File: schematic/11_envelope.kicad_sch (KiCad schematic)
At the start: 23 parts, among them Q601 2N7002, Q602 MMBT3904, Q603 BSS84, Q604 MMBT3904, Q605 2N7002, U601 TLC555IDR, U602 OPA4192IDR

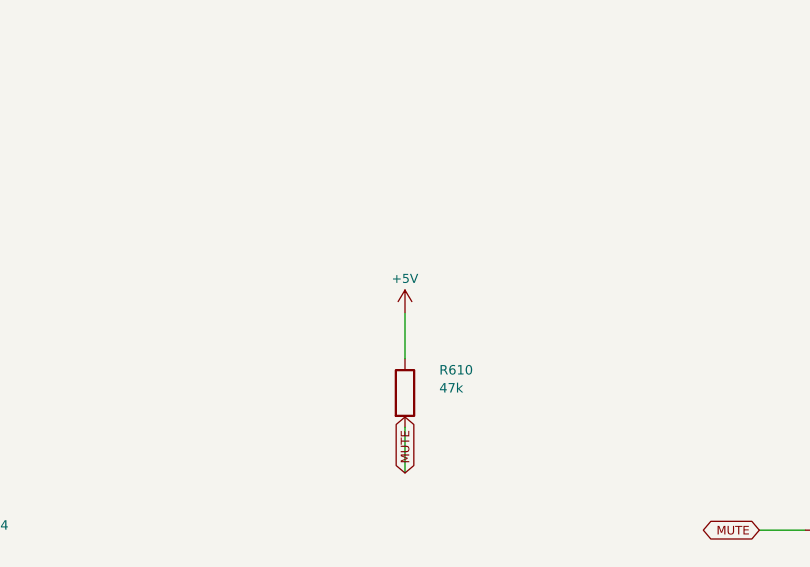
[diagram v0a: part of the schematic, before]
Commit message: add power supply, rail checks and parts list
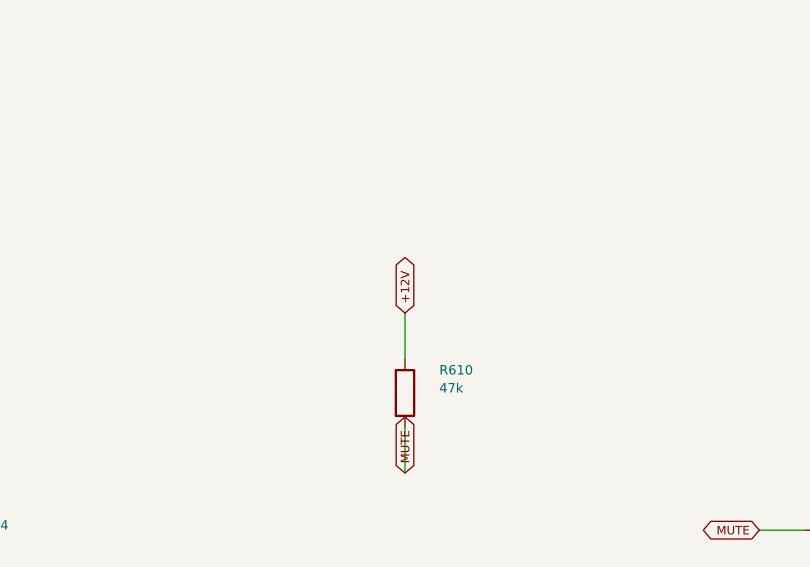
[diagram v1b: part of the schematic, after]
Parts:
- Q601, Q605: MPN (none) -> 2N7002,215; Manufacturer (none) -> Nexperia; Supplier (none) -> LCSC
- Q602, Q604: MPN (none) -> MMBT3904,215; Manufacturer (none) -> Nexperia; Supplier (none) -> LCSC
- Q603: MPN (none) -> BSS84,215; Manufacturer (none) -> Nexperia; Supplier (none) -> LCSC
- U601: MPN (none) -> TLC555IDR; Manufacturer (none) -> Texas Instruments; Supplier (none) -> LCSC
- U602: MPN (none) -> OPA4192IDR; Manufacturer (none) -> Texas Instruments; Supplier (none) -> LCSC; Supplier URL (none) -> https://www.lcsc.com/product-detail/C2057908.html
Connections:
- net +5V: no longer R610.1
- new net +12V: R610.1
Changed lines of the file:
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@@
+      )
+    )
+    (property "MPN" "OPA4192IDR"
+      (at 335.28 214.63 0.0)
+      (effects
+        (font
+          (size 1.0 1.0)
+        )
+        (hide yes)
+      )
+    )
+    (property "Manufacturer" "Texas Instruments"
+      (at 335.28 214.63 0.0)
+      (effects
+        (font
+          (size 1.0 1.0)
+        )
+        (hide yes)
+      )
+    )
+    (property "Supplier" "LCSC"
+      (at 335.28 214.63 0.0)
+      (effects
+        (font
+          (size 1.0 1.0)
+        )
+        (hide yes)
+      )
+    )
+    (property "Supplier URL" "https://www.lcsc.com/product-detail/C2057908.html"
+      (at 335.28 214.63 0.0)
+      (effects
+        (font
+          (size 1.0 1.0)
+        )
+        (hide yes)
       )
     )
@@
       )
     )
-    (property "Datasheet" "https://www.onsemi.com/pub/Collateral/NDS7002A-D.PDF"
+    (property "Datasheet" "https://assets.nexperia.com/documents/data-sheet/2N7002.pdf"
       (at 53.34 62.23 0.0)
       (effects
@@
         )
         (justify left)
+        (hide yes)
+      )
+    )
+    (property "MPN" "2N7002,215"
+      (at 49.53 64.77 0.0)
+      (effects
+        (font
+          (size 1.0 1.0)
+        )
+        (hide yes)
+      )
+    )
+    (property "Manufacturer" "Nexperia"
+      (at 49.53 64.77 0.0)
+      (effects
+        (font
+          (size 1.0 1.0)
+        )
+        (hide yes)
+      )
+    )
+    (property "Supplier" "LCSC"
+      (at 49.53 64.77 0.0)
+      (effects
+        (font
+          (size 1.0 1.0)
+        )
         (hide yes)
       )
@@
       )
     )
-    (property "Datasheet" "http://www.ti.com/lit/ds/symlink/tlc555.pdf"
+    (property "Datasheet" "https://www.ti.com/lit/ds/symlink/tlc555.pdf"
       (at 137.16 46.99 0.0)
       (effects
@@
         )
         (justify left)
+        (hide yes)
+      )
+    )
+    (property "MPN" "TLC555IDR"
+      (at 154.94 64.77 0.0)
+      (effects
+        (font
+          (size 1.0 1.0)
+        )
+        (hide yes)
+      )
+    )
+    (property "Manufacturer" "Texas Instruments"
+      (at 154.94 64.77 0.0)
+      (effects
+        (font
+          (size 1.0 1.0)
+        )
+        (hide yes)
+      )
+    )
+    (property "Supplier" "LCSC"
+      (at 154.94 64.77 0.0)
+      (effects
+        (font
+          (size 1.0 1.0)
+        )
         (hide yes)
       )
@@
       )
     )
-    (property "Datasheet" "https://www.onsemi.com/pdf/datasheet/pzt3904-d.pdf"
+    (property "Datasheet" "https://assets.nexperia.com/documents/data-sheet/MMBT3904.pdf"
       (at 323.85 62.23 0.0)
       (effects
@@
         )
         (justify left)
+        (hide yes)
+      )
+    )
+    (property "MPN" "MMBT3904,215"
+      (at 320.04 64.77 0.0)
+      (effects
+        (font
+          (size 1.0 1.0)
+        )
+        (hide yes)
+      )
+    )
+    (property "Manufacturer" "Nexperia"
+      (at 320.04 64.77 0.0)
+      (effects
+        (font
+          (size 1.0 1.0)
+        )
+        (hide yes)
+      )
+    )
+    (property "Supplier" "LCSC"
+      (at 320.04 64.77 0.0)
+      (effects
+        (font
+          (size 1.0 1.0)
+        )
         (hide yes)
       )
@@
       )
     )
-    (property "Datasheet" "http://assets.nexperia.com/documents/data-sheet/BSS84.pdf"
+    (property "Datasheet" "https://assets.nexperia.com/documents/data-sheet/BSS84.pdf"
       (at 368.3 113.02999999999999 0.0)
       (effects
@@
         )
         (justify left)
+        (hide yes)
+      )
+    )
+    (property "MPN" "BSS84,215"
+      (at 364.49 115.57 0.0)
+      (effects
+        (font
+          (size 1.0 1.0)
+        )
+        (hide yes)
+      )
+    )
+    (property "Manufacturer" "Nexperia"
+      (at 364.49 115.57 0.0)
+      (effects
+        (font
+          (size 1.0 1.0)
+        )
+        (hide yes)
+      )
+    )
+    (property "Supplier" "LCSC"
+      (at 364.49 115.57 0.0)
+      (effects
+        (font
+          (size 1.0 1.0)
+        )
         (hide yes)
       )
@@
       )
     )
-    (property "Datasheet" "https://www.onsemi.com/pdf/datasheet/pzt3904-d.pdf"
+    (property "Datasheet" "https://assets.nexperia.com/documents/data-sheet/MMBT3904.pdf"
       (at 123.19 262.89 0.0)
       (effects
@@
         )
         (justify left)
+        (hide yes)
+      )
+    )
+    (property "MPN" "MMBT3904,215"
+      (at 119.38 265.43 0.0)
+      (effects
+        (font
+          (size 1.0 1.0)
+        )
+        (hide yes)
+      )
+    )
+    (property "Manufacturer" "Nexperia"
+      (at 119.38 265.43 0.0)
+      (effects
+        (font
+          (size 1.0 1.0)
+        )
+        (hide yes)
+      )
+    )
+    (property "Supplier" "LCSC"
+      (at 119.38 265.43 0.0)
+      (effects
+        (font
+          (size 1.0 1.0)
+        )
         (hide yes)
       )
@@
     )
   )
-  (symbol
-    (lib_id "power:+5V")
-    (at 175.26 241.3 0.0)
-    (unit 1)
-    (exclude_from_sim no)
-    (in_bom no)
-    (on_board no)
-    (dnp no)
-    (property "Reference" "#PWR19099"
-      (at 175.26 241.3 0.0)
-      (effects
-        (font
-          (size 1.0 1.0)
-        )
-        (hide yes)
-      )
-    )
-    (property "Value" "+5V"
-      (at 175.26 237.49 0.0)
-      (effects
-        (font
-          (size 1.0 1.0)
-        )
-      )
-    )
-    (instances
-      (project "arpeggiator"
-        (path "/b74f2899-8338-4c76-a1a7-8fd841787321/9c41fc11-054f-50f6-9bdd-e2a135d8b814"
-          (reference "#PWR19099")
-          (unit 1)
-        )
-      )
+  (global_label "+12V"
+    (shape bidirectional)
+    (at 175.26 241.3 90.0)
+    (effects
+      (font
+        (size 0.95 0.95)
+      )
+      (justify left)
     )
   )
@@
       )
     )
-    (property "Datasheet" "https://www.onsemi.com/pub/Collateral/NDS7002A-D.PDF"
+    (property "Datasheet" "https://assets.nexperia.com/documents/data-sheet/2N7002.pdf"
       (at 228.6 262.89 0.0)
       (effects
@@
         (hide yes)
       )
+    )
+    (property "MPN" "2N7002,215"
+      (at 224.79 265.43 0.0)
+      (effects
+        (font
+          (size 1.0 1.0)
+        )
+        (hide yes)
+      )
+    )
+    (property "Manufacturer" "Nexperia"
+      (at 224.79 265.43 0.0)
+      (effects
+        (font
+          (size 1.0 1.0)
+        )
+        (hide yes)
+      )
+    )
+    (property "Supplier" "LCSC"
+      (at 224.79 265.43 0.0)
+      (effects
+        (font
+          (size 1.0 1.0)
+        )
+        (hide yes)
+      )

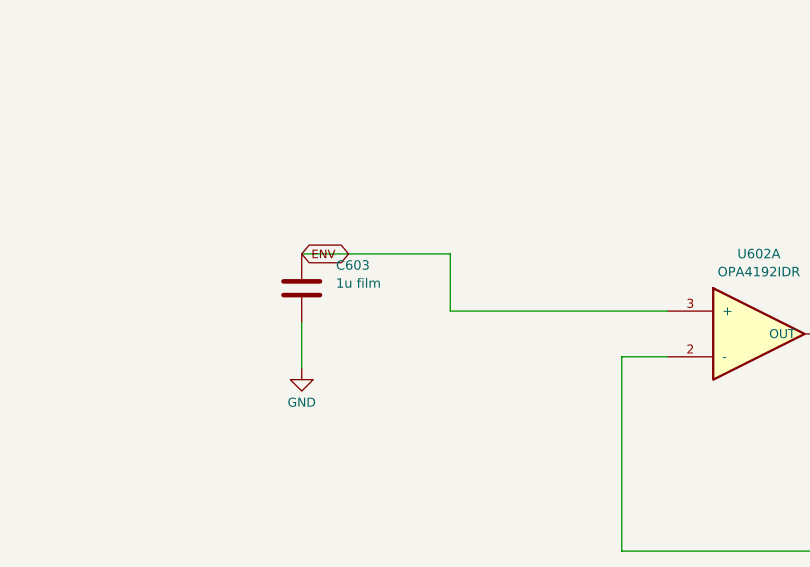
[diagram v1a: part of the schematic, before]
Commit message: pick controls and start pcb placement
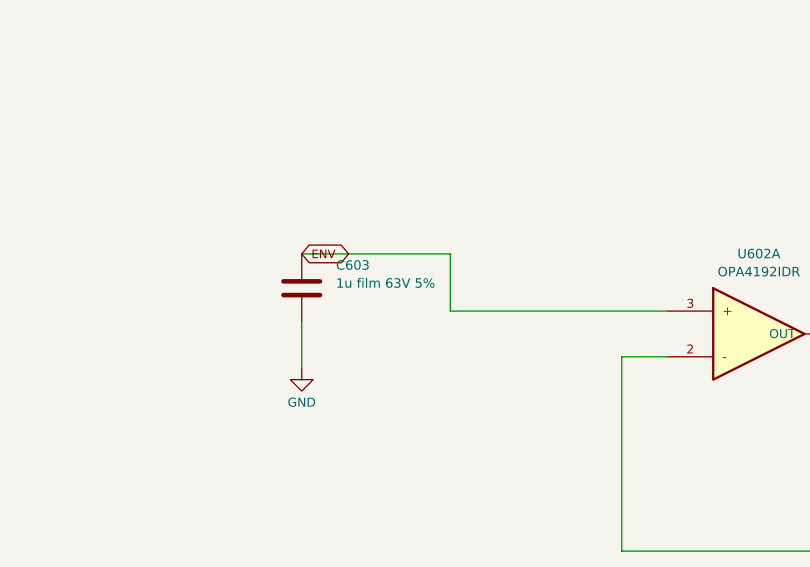
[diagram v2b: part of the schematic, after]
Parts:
- C603: value 1u film -> 1u film 63V 5%; footprint (none) -> Capacitor_THT:C_Rect_L7.2mm_W5.0mm_P5.00mm; MPN (none) -> R82DC4100DQ60J; Manufacturer (none) -> KEMET; Supplier (none) -> Tayda; Supplier URL (none) -> https://www.taydaelectronics.com/1uf-63v-5-kemet-polyester-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
- RV601: footprint (none) -> Potentiometer_THT:Potentiometer_Alpha_RD901F-40-00D_Single_Vertical; MPN (none) -> RD901F-40-15F-B1M; Manufacturer (none) -> Taiwan Alpha; Supplier (none) -> Tayda; Supplier URL (none) -> https://www.taydaelectronics.com/potentiometer-variable-res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
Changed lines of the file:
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@@
       )
     )
-    (property "Value" "1u film"
+    (property "Value" "1u film 63V 5%"
       (at 288.29 209.01000000000002 0.0)
       (effects
@@
       )
     )
-    (property "Footprint" ""
+    (property "Footprint" "Capacitor_THT:C_Rect_L7.2mm_W5.0mm_P5.00mm"
       (at 288.29 207.01000000000002 0.0)
       (effects
@@
         )
         (justify left)
+        (hide yes)
+      )
+    )
+    (property "MPN" "R82DC4100DQ60J"
+      (at 284.48 209.55 0.0)
+      (effects
+        (font
+          (size 1.0 1.0)
+        )
+        (hide yes)
+      )
+    )
+    (property "Manufacturer" "KEMET"
+      (at 284.48 209.55 0.0)
+      (effects
+        (font
+          (size 1.0 1.0)
+        )
+        (hide yes)
+      )
+    )
+    (property "Supplier" "Tayda"
+      (at 284.48 209.55 0.0)
+      (effects
+        (font
+          (size 1.0 1.0)
+        )
+        (hide yes)
+      )
+    )
+    (property "Supplier URL" "https://www.taydaelectronics.com/1uf-63v-5-kemet-polyester-film-box-type-capacitor.html"
+      (at 284.48 209.55 0.0)
+      (effects
+        (font
+          (size 1.0 1.0)
+        )
         (hide yes)
       )
@@
       )
     )
-    (property "Footprint" ""
+    (property "Footprint" "Potentiometer_THT:Potentiometer_Alpha_RD901F-40-00D_Single_Vertical"
       (at 64.77 200.66000000000003 0.0)
       (effects
@@
       )
     )
-    (property "Datasheet" ""
+    (property "Datasheet" "https://www.taydaelectronics.com/datasheets/files/A-4728-1.pdf"
       (at 64.77 200.66000000000003 0.0)
       (effects
@@
         (hide yes)
       )
+    )
+    (property "MPN" "RD901F-40-15F-B1M"
+      (at 95.25 209.55 0.0)
+      (effects
+        (font
+          (size 1.0 1.0)
+        )
+        (hide yes)
+      )
+    )
+    (property "Manufacturer" "Taiwan Alpha"
+      (at 95.25 209.55 0.0)
+      (effects
+        (font
+          (size 1.0 1.0)
+        )
+        (hide yes)
+      )
+    )
+    (property "Supplier" "Tayda"
+      (at 95.25 209.55 0.0)
+      (effects
+        (font
+          (size 1.0 1.0)
+        )
+        (hide yes)
+      )
+    )
+    (property "Supplier URL" "https://www.taydaelectronics.com/potentiometer-variable-resistors/rotary-potentiometer/linear/1m-ohm-linear-taper-potentiometer-d-shaft-pcb-9mm.html"
+      (at 95.25 209.55 0.0)
+      (effects
+        (font
+          (size 1.0 1.0)
+        )
+        (hide yes)
+      )
